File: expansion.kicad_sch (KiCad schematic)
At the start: 2 parts, among them J3 EXPANSION, J5 Solder Pads

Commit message: Added expansion connectors to pcb
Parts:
- J3: footprint (none) -> tuxkeychain:FFC_1x15_P0.5mm
- J5: footprint (none) -> Connector_PinHeader_1.00mm:PinHeader_1x12_P1.00mm_Vertical_SMD_Pin1Left
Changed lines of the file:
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@@
 			)
 		)
-		(property "Footprint" ""
+		(property "Footprint" "tuxkeychain:FFC_1x15_P0.5mm"
 			(at 133.35 113.03 0)
 			(effects
@@
 			)
 		)
-		(property "Footprint" ""
+		(property "Footprint" "Connector_PinHeader_1.00mm:PinHeader_1x12_P1.00mm_Vertical_SMD_Pin1Left"
 			(at 195.58 95.25 0)
 			(effects

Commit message: work
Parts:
- J5: footprint Connector_PinHeader_1.00mm:PinHeader_1x12_P1.00mm_Vertical_SMD_Pin1Left -> tuxkeychain:SolderPads12
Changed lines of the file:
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@@
 			)
 		)
-		(property "Footprint" "Connector_PinHeader_1.00mm:PinHeader_1x12_P1.00mm_Vertical_SMD_Pin1Left"
+		(property "Footprint" "tuxkeychain:SolderPads12"
 			(at 195.58 95.25 0)
 			(effects

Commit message: fix name for footprint
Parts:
- J3: footprint tuxkeychain:FFC_1x15_P0.5mm -> tuxkeychain:Jushuo_AFC07-S15FCA-00_1x15-1MP_P0.50_Horizontal
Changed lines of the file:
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@@
 			)
 		)
-		(property "Footprint" "tuxkeychain:FFC_1x15_P0.5mm"
+		(property "Footprint" "tuxkeychain:Jushuo_AFC07-S15FCA-00_1x15-1MP_P0.50_Horizontal"
 			(at 133.35 113.03 0)
 			(effects

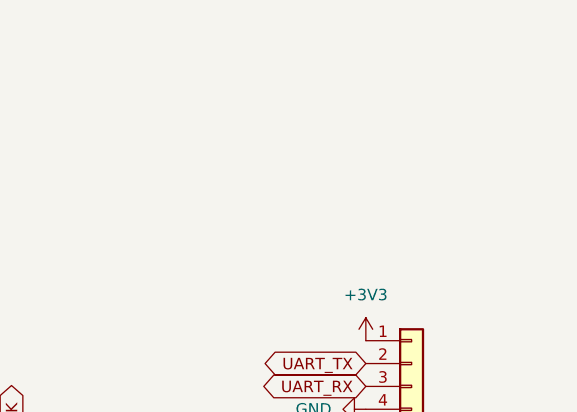
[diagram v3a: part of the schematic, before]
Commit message: add uart header
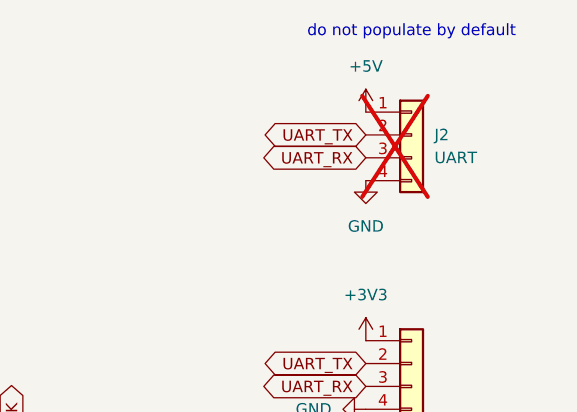
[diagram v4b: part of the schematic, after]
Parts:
- added J2: UART, Connector_PinHeader_2.54mm:PinHeader_1x04_P2.54mm_Vertical_SMD_Pin1Left, symbol Connector_Generic:Conn_01x04
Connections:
- net +5V: now also J2.1 (Pin_1)
- net GND: now also J2.4 (Pin_4)
- net UART_RX: now also J2.3 (Pin_3)
- net UART_TX: now also J2.2 (Pin_2)
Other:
- note added: "do not populate by default"
